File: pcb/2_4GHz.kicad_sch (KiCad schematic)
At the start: 15 parts, among them J2 USB_A, U1 ATtiny85-20P, U2 LP2950-3.3_TO92, U3 NRF24L01_Breakout_8P

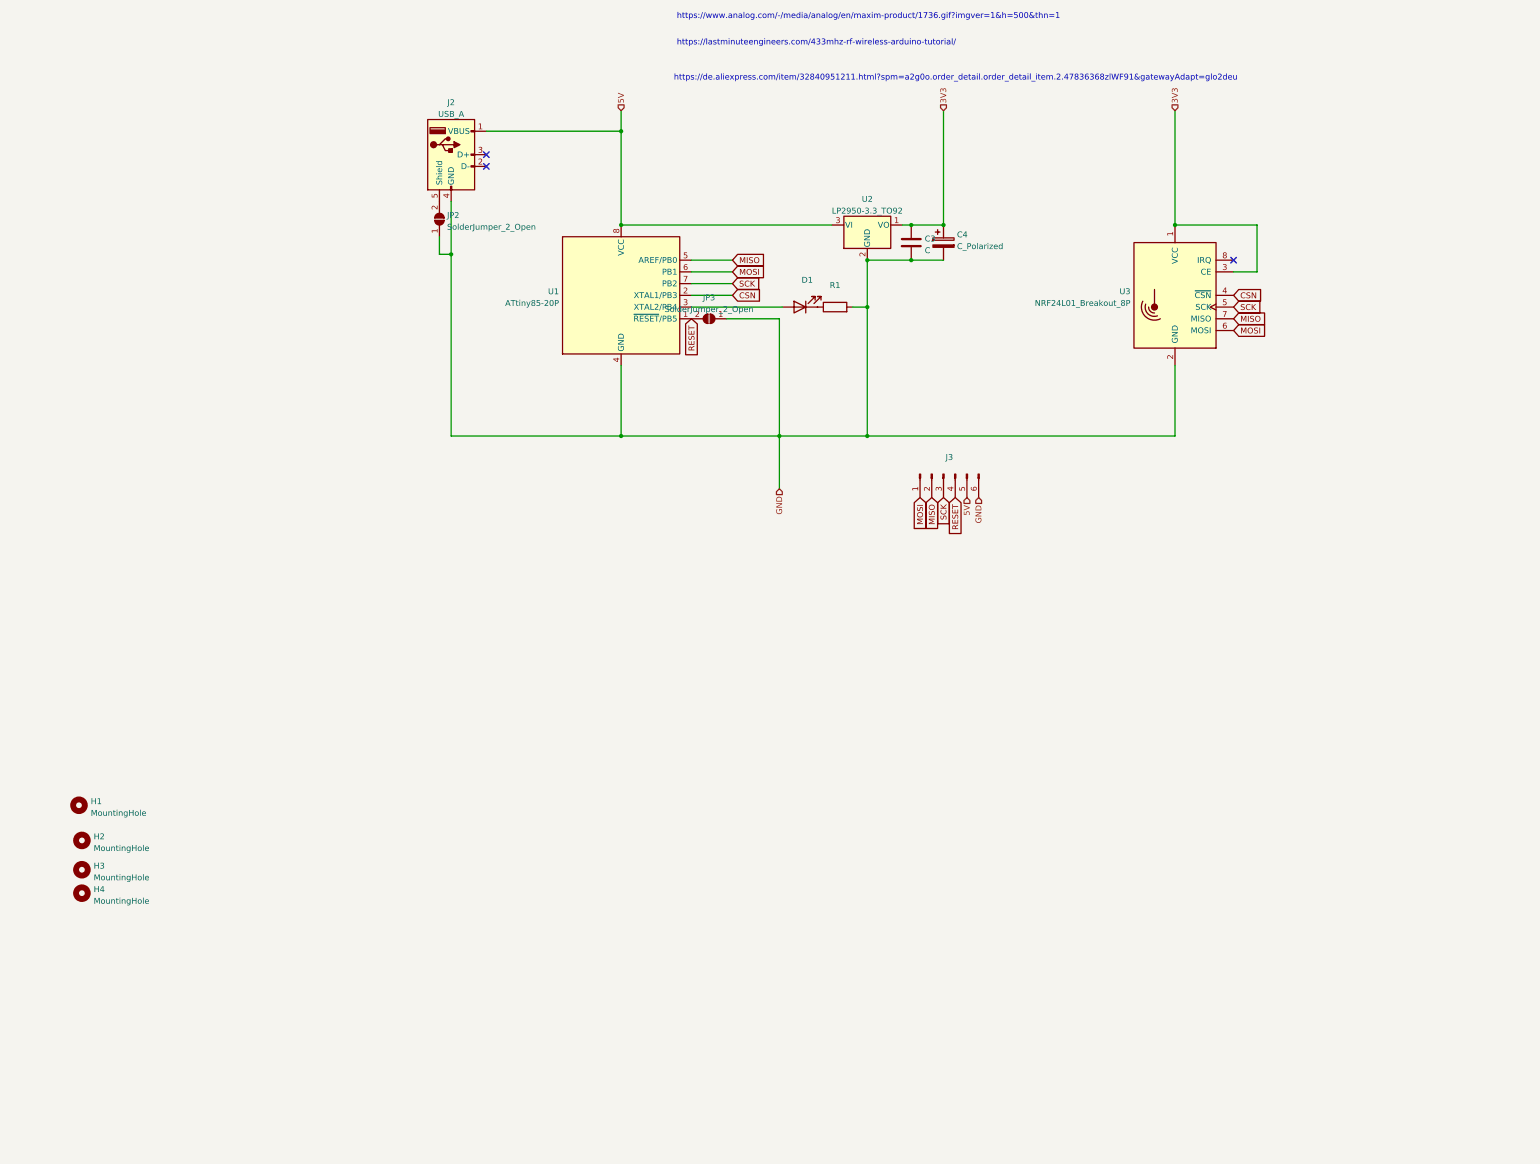
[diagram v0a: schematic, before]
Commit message: Update PCB to Arduino UNO and Nano
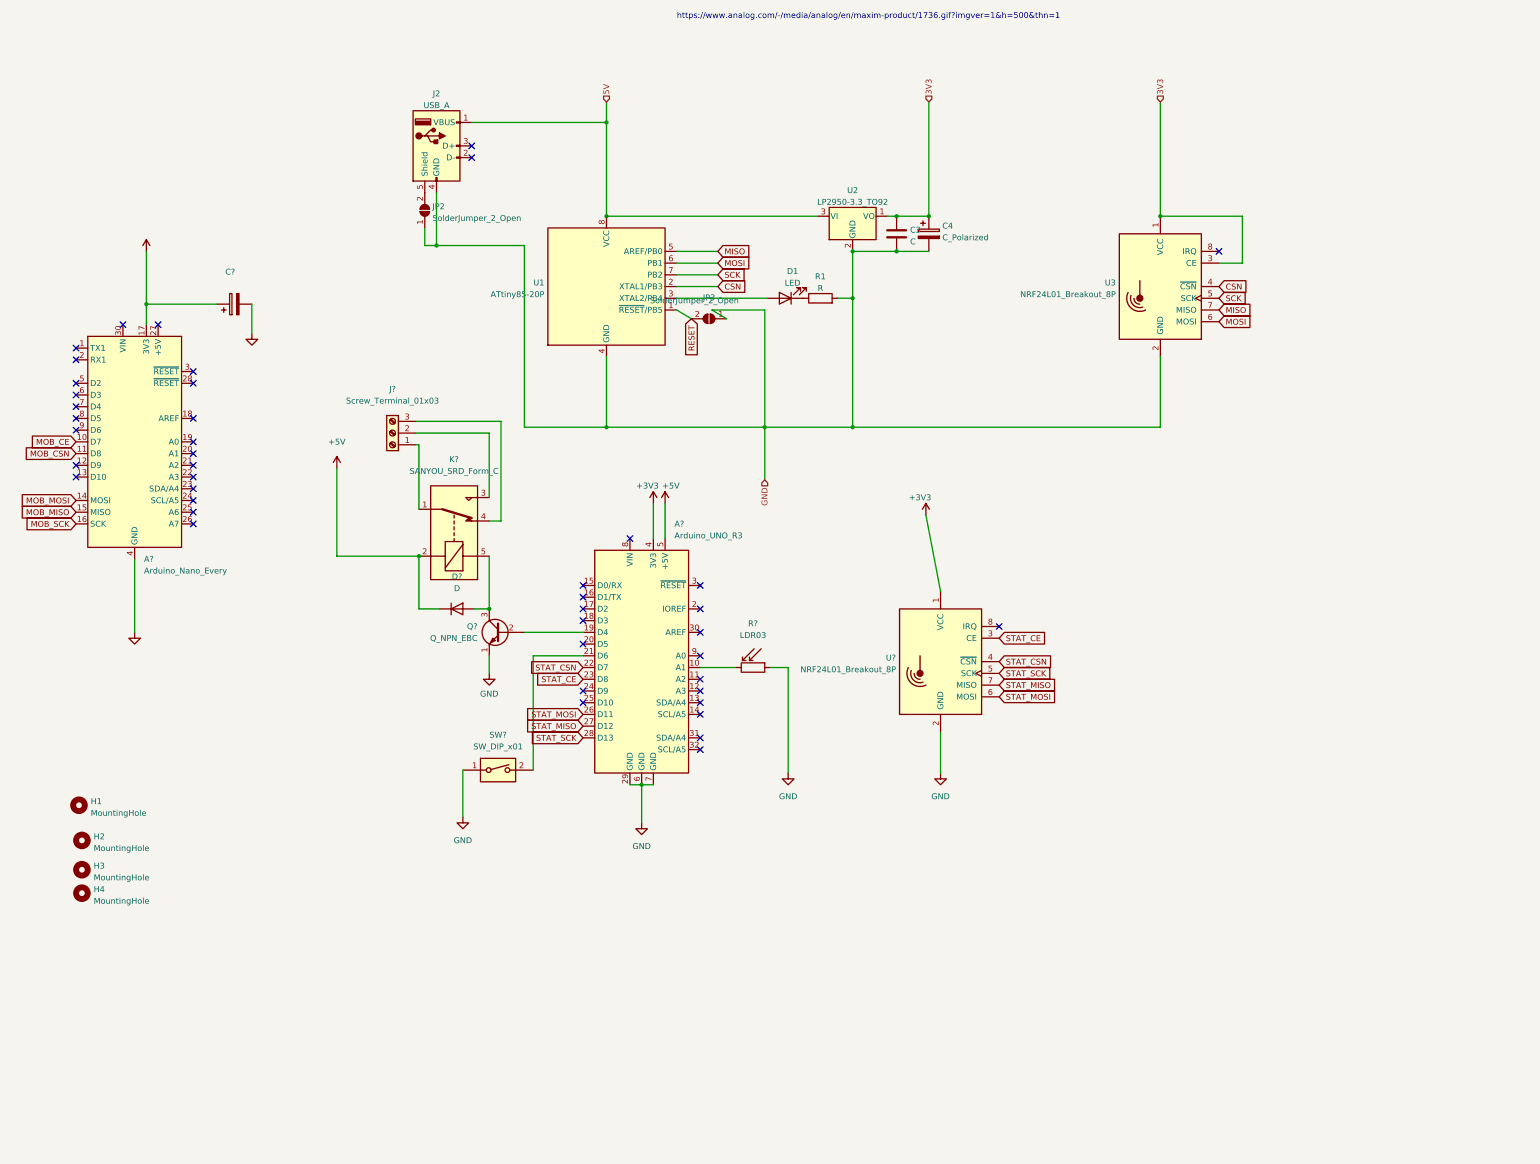
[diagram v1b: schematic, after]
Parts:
- removed J3: (no value), symbol Connector:Conn_01x06_Male
- added A?: Arduino_Nano_Every, Module:Arduino_Nano, symbol MCU_Module:Arduino_Nano_Every
- added A?: Arduino_UNO_R3, Module:Arduino_UNO_R3, symbol MCU_Module:Arduino_UNO_R3
- added C?: (no value), symbol Device:C_Polarized
- added D?: D, symbol Device:D
- added J?: Screw_Terminal_01x03, symbol Connector:Screw_Terminal_01x03
- added K?: SANYOU_SRD_Form_C, Relay_THT:Relay_SPDT_SANYOU_SRD_Series_Form_C, symbol Relay:SANYOU_SRD_Form_C
- added Q?: Q_NPN_EBC, symbol Device:Q_NPN_EBC
- added R?: LDR03, OptoDevice:R_LDR_10x8.5mm_P7.6mm_Vertical, symbol Sensor_Optical:LDR03
- added SW?: SW_DIP_x01, symbol Switch:SW_DIP_x01
- added U?: NRF24L01_Breakout_8P, RF_Module:NRF24L01-Module-SMD, symbol RF:NRF24L01_Breakout_8P
- D1: value (none) -> LED; footprint (none) -> LED_THT:LED_D3.0mm
- JP3: footprint (none) -> Jumper:SolderJumper-2_P1.3mm_Open_Pad1.0x1.5mm
- R1: value (none) -> R; footprint (none) -> Resistor_SMD:R_2010_5025Metric_Pad1.40x2.65mm_HandSolder
- U1: footprint (none) -> Package_SO:SOP-8_3.76x4.96mm_P1.27mm
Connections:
- net GND: now also A?.29 (GND), A?.29 (GND), A?.4 (GND), A?.6 (GND), A?.7 (GND), C?.2, Q?.1 (E), R?.1, SW?.1, U?.2 (GND)
- new net: A?.19 (D4), Q?.2 (B)
- new net: D?.2 (A), K?.5, Q?.3 (C)
- new net: A?.10 (A1), R?.2
- new net: A?.21 (D6), SW?.2
- new net: J?.1 (Pin_1), K?.1
- new net: J?.2 (Pin_2), K?.3
- new net: J?.3 (Pin_3), K?.4
- new net +3V3: A?.17 (3V3), A?.4 (3V3), C?.1, U?.1 (VCC)
- new net +5V: A?.5 (+5V), D?.1 (K), K?.2
- new net MOB_CE: A?.10 (D7)
- new net MOB_CSN: A?.11 (D8)
- new net MOB_MISO: A?.15 (MISO)
- new net MOB_MOSI: A?.14 (MOSI)
- new net MOB_SCK: A?.16 (SCK)
- new net STAT_CE: A?.23 (D8), U?.3 (CE)
- new net STAT_CSN: A?.22 (D7), U?.4 (~{CSN})
- new net STAT_MISO: A?.27 (D12), U?.7 (MISO)
- new net STAT_MOSI: A?.26 (D11), U?.6 (MOSI)
- new net STAT_SCK: A?.28 (D13), U?.5 (SCK)
- no-connect marks 3 -> 44
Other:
- note removed: "https://de.aliexpress.com/item/32840951211.html?spm=a2g0o.order_detail.order_detail_item.2.47836368zlWF91&gatewayAdapt=glo2deu"
- note removed: "https://lastminuteengineers.com/433mhz-rf-wireless-arduino-tutorial/"
- moved on the sheet: C3, C4, D1, J2, JP2, R1, U1, U2, U3

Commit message: NRF works on Nano with PA_MAX power now
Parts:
- added C1: 470uF, symbol Device:C_Polarized
- added C2: 70nF, symbol Device:C
- added C6: 4.7uF, symbol Device:C_Polarized
- added SW1: SW_DPDT_x2, symbol Switch:SW_DPDT_x2
- added U4: LP2950-3.3_TO92, Package_TO_SOT_THT:TO-92_Inline, symbol Regulator_Linear:LP2950-3.3_TO92
- C?: value (none) -> C_Polarized
- gave numbers to parts that had none: 1
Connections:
- net +3V3: now also SW1.3 (C); no longer U5.1 (VCC)
- net +5V: now also C1.1, C2.1, U4.3 (VI)
- net GND: now also C1.2, C2.2, C6.2, U4.2 (GND)
- new net: C6.1, SW1.1 (A), U4.1 (VO)
- new net: SW1.2 (B), U5.1 (VCC)
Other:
- note added: "Von Arduino Nano"
- moved on the sheet: A?, D?, J?, K?, Q?, R?, SW?, U5
